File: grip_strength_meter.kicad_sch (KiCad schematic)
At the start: 0 parts

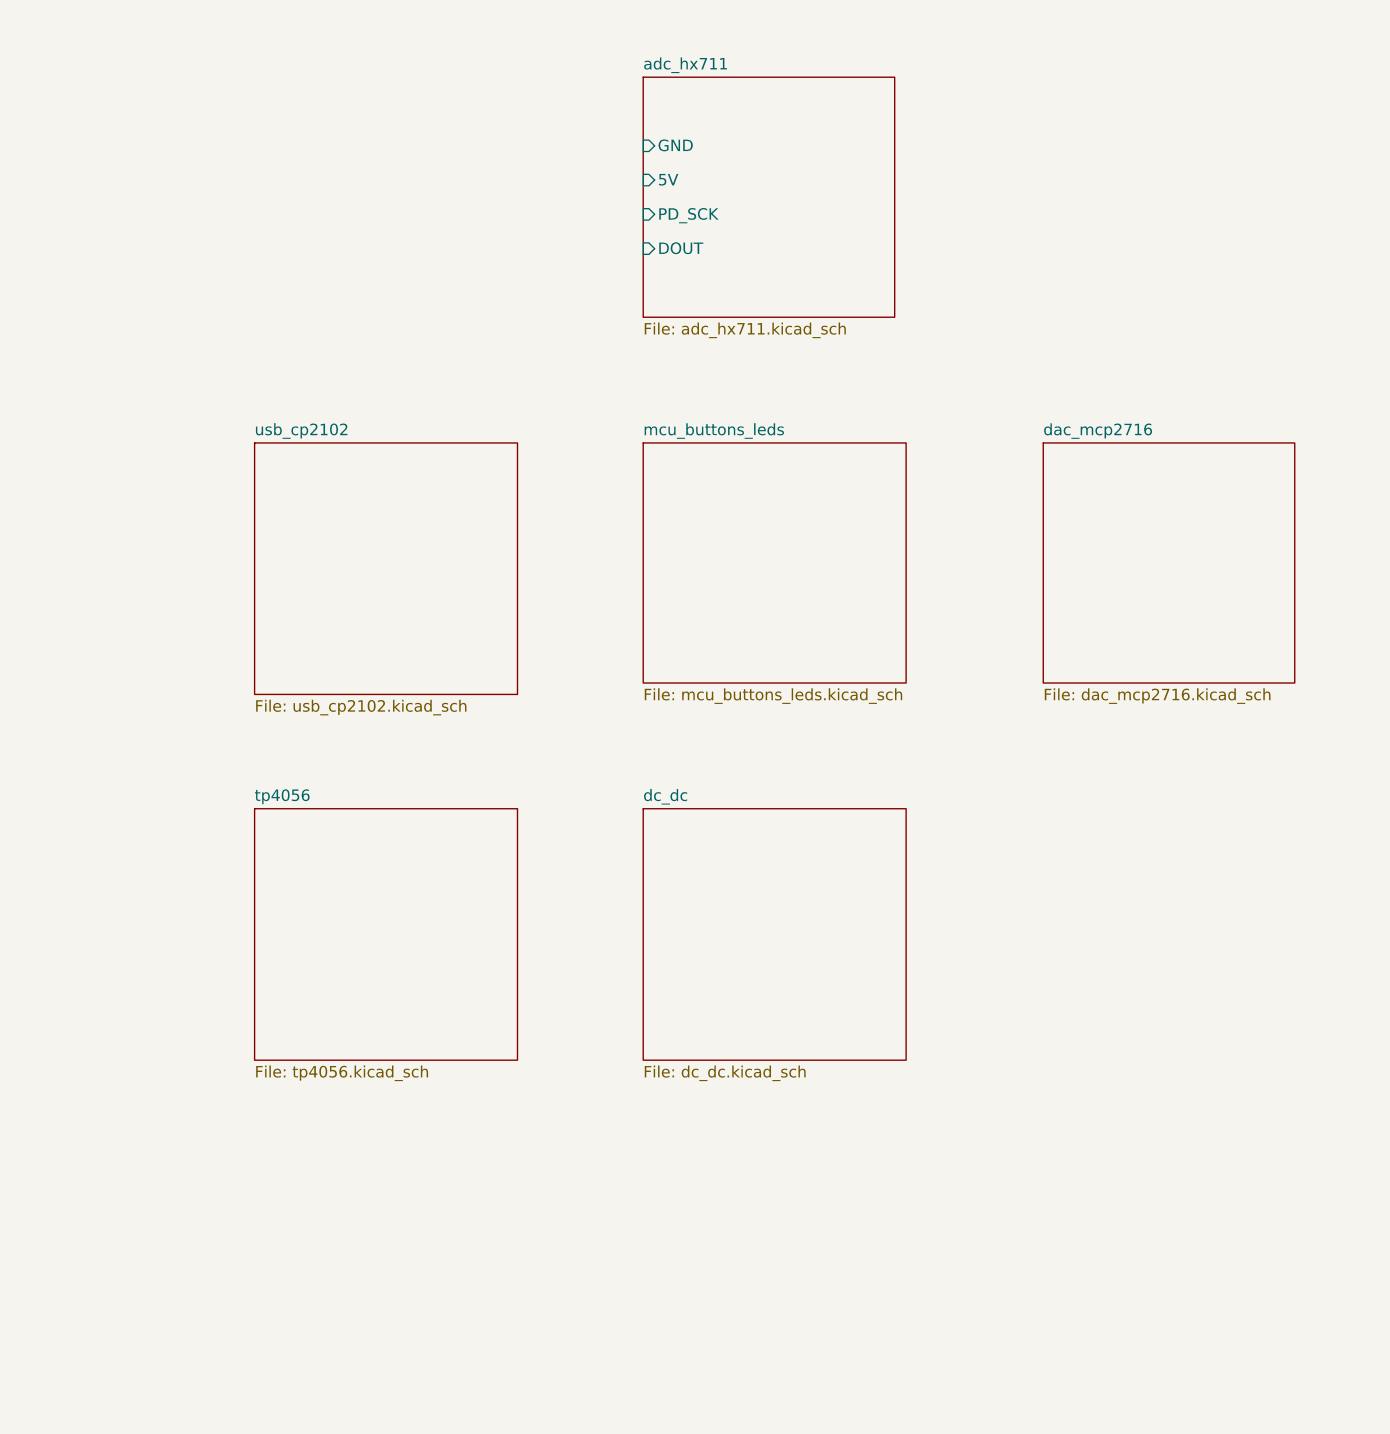
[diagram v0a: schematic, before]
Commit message: added cp2102 schematics
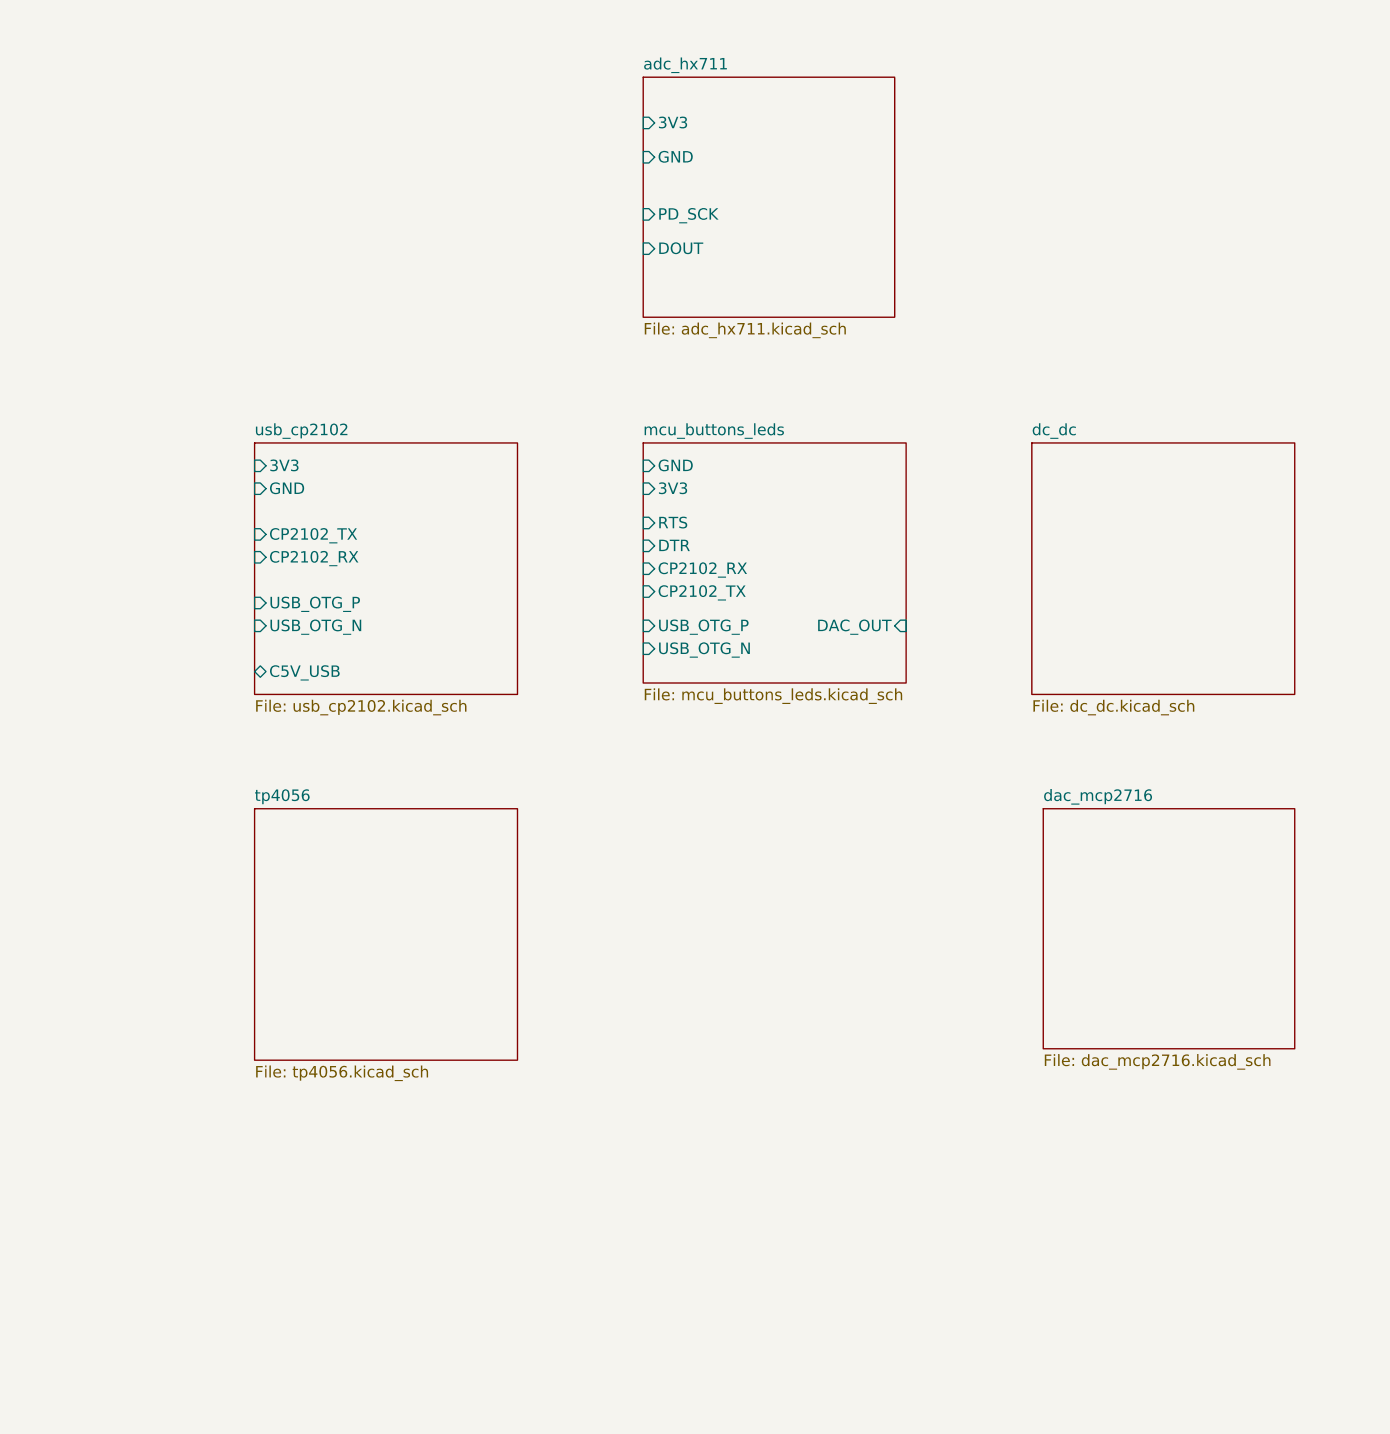
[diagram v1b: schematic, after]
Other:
- sheet adc_hx711 ports: added 3V3; removed 5V
- sheet mcu_buttons_leds ports: added 3V3, CP2102_RX, CP2102_TX, DAC_OUT, DTR, GND, RTS, USB_OTG_N, USB_OTG_P; removed none
- sheet usb_cp2102 ports: added 3V3, C5V_USB, CP2102_RX, CP2102_TX, GND, USB_OTG_N, USB_OTG_P; removed none
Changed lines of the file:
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@@
       (effects (font (size 1.27 1.27)) (justify left top))
+    )
+    (pin "GND" input (at 92.71 82.55 180)
+      (effects (font (size 1.27 1.27)) (justify left))
+    )
+    (pin "3V3" input (at 92.71 85.09 180)
+      (effects (font (size 1.27 1.27)) (justify left))
+    )
+    (pin "RTS" input (at 92.71 88.9 180)
+      (effects (font (size 1.27 1.27)) (justify left))
+    )
+    (pin "DTR" input (at 92.71 91.44 180)
+      (effects (font (size 1.27 1.27)) (justify left))
+    )
+    (pin "DAC_OUT" input (at 121.92 100.33 0)
+      (effects (font (size 1.27 1.27)) (justify right))
+    )
+    (pin "USB_OTG_P" input (at 92.71 100.33 180)
+      (effects (font (size 1.27 1.27)) (justify left))
+    )
+    (pin "USB_OTG_N" input (at 92.71 102.87 180)
+      (effects (font (size 1.27 1.27)) (justify left))
+    )
+    (pin "CP2102_RX" input (at 92.71 93.98 180)
+      (effects (font (size 1.27 1.27)) (justify left))
+    )
+    (pin "CP2102_TX" input (at 92.71 96.52 180)
+      (effects (font (size 1.27 1.27)) (justify left))
     )
     (instances
@@
     )
   )
-  (sheet (at 92.71 120.65) (size 29.21 27.94) (fields_autoplaced)
+  (sheet (at 135.89 80.01) (size 29.21 27.94) (fields_autoplaced)
     (stroke (width 0.1524) (type solid))
     (fill (color 0 0 0 0.0000))
-    (property "Sheetname" "dc_dc" (at 92.71 119.9384 0)
+    (property "Sheetname" "dc_dc" (at 135.89 79.2984 0)
       (effects (font (size 1.27 1.27)) (justify left bottom))
     )
-    (property "Sheetfile" "dc_dc.kicad_sch" (at 92.71 149.1746 0)
+    (property "Sheetfile" "dc_dc.kicad_sch" (at 135.89 108.5346 0)
       (effects (font (size 1.27 1.27)) (justify left top))
     )
@@
     )
   )
-  (sheet (at 137.16 80.01) (size 27.94 26.67) (fields_autoplaced)
+  (sheet (at 137.16 120.65) (size 27.94 26.67) (fields_autoplaced)
     (stroke (width 0.1524) (type solid))
     (fill (color 0 0 0 0.0000))
-    (property "Sheetname" "dac_mcp2716" (at 137.16 79.2984 0)
+    (property "Sheetname" "dac_mcp2716" (at 137.16 119.9384 0)
       (effects (font (size 1.27 1.27)) (justify left bottom))
     )
-    (property "Sheetfile" "dac_mcp2716.kicad_sch" (at 137.16 107.2646 0)
+    (property "Sheetfile" "dac_mcp2716.kicad_sch" (at 137.16 147.9046 0)
       (effects (font (size 1.27 1.27)) (justify left top))
     )
@@
       (effects (font (size 1.27 1.27)) (justify left top))
     )
-    (pin "GND" input (at 92.71 46.99 180)
-      (effects (font (size 1.27 1.27)) (justify left))
-    )
-    (pin "5V" input (at 92.71 50.8 180)
+    (pin "GND" input (at 92.71 48.26 180)
       (effects (font (size 1.27 1.27)) (justify left))
     )
@@
     )
     (pin "DOUT" input (at 92.71 58.42 180)
+      (effects (font (size 1.27 1.27)) (justify left))
+    )
+    (pin "3V3" input (at 92.71 44.45 180)
       (effects (font (size 1.27 1.27)) (justify left))
     )
@@
       (effects (font (size 1.27 1.27)) (justify left top))
     )
+    (pin "3V3" input (at 49.53 82.55 180)
+      (effects (font (size 1.27 1.27)) (justify left))
+    )
+    (pin "GND" input (at 49.53 85.09 180)
+      (effects (font (size 1.27 1.27)) (justify left))
+    )
+    (pin "USB_OTG_P" input (at 49.53 97.79 180)
+      (effects (font (size 1.27 1.27)) (justify left))
+    )
+    (pin "C5V_USB" bidirectional (at 49.53 105.41 180)
+      (effects (font (size 1.27 1.27)) (justify left))
+    )
+    (pin "USB_OTG_N" input (at 49.53 100.33 180)
+      (effects (font (size 1.27 1.27)) (justify left))
+    )
+    (pin "CP2102_TX" input (at 49.53 90.17 180)
+      (effects (font (size 1.27 1.27)) (justify left))
+    )
+    (pin "CP2102_RX" input (at 49.53 92.71 180)
+      (effects (font (size 1.27 1.27)) (justify left))
+    )
     (instances

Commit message: schematics almost finished
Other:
- removed sheet dc_dc
- sheet tp4056 ports: added 3V3, C5V_USB, GND, GPIO_BUTTON_CHECK, GPIO_POWEROFF, V_BAT, V_BAT_MEASURE; removed none
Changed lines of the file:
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@@
     )
   )
-  (sheet (at 49.53 120.65) (size 29.21 27.94) (fields_autoplaced)
+  (sheet (at 137.16 80.01) (size 29.21 27.94) (fields_autoplaced)
     (stroke (width 0.1524) (type solid))
     (fill (color 0 0 0 0.0000))
-    (property "Sheetname" "tp4056" (at 49.53 119.9384 0)
+    (property "Sheetname" "tp4056" (at 137.16 79.2984 0)
       (effects (font (size 1.27 1.27)) (justify left bottom))
     )
-    (property "Sheetfile" "tp4056.kicad_sch" (at 49.53 149.1746 0)
+    (property "Sheetfile" "tp4056.kicad_sch" (at 137.16 108.5346 0)
       (effects (font (size 1.27 1.27)) (justify left top))
+    )
+    (pin "GPIO_BUTTON_CHECK" input (at 137.16 82.55 180)
+      (effects (font (size 1.27 1.27)) (justify left))
+    )
+    (pin "GPIO_POWEROFF" input (at 137.16 85.09 180)
+      (effects (font (size 1.27 1.27)) (justify left))
+    )
+    (pin "C5V_USB" bidirectional (at 137.16 87.63 180)
+      (effects (font (size 1.27 1.27)) (justify left))
+    )
+    (pin "GND" input (at 137.16 90.17 180)
+      (effects (font (size 1.27 1.27)) (justify left))
+    )
+    (pin "3V3" input (at 137.16 92.71 180)
+      (effects (font (size 1.27 1.27)) (justify left))
+    )
+    (pin "V_BAT" input (at 137.16 95.25 180)
+      (effects (font (size 1.27 1.27)) (justify left))
+    )
+    (pin "V_BAT_MEASURE" input (at 137.16 97.79 180)
+      (effects (font (size 1.27 1.27)) (justify left))
     )
     (instances
@@
       )
     )
-  )
-  (sheet (at 135.89 80.01) (size 29.21 27.94) (fields_autoplaced)
-    (stroke (width 0.1524) (type solid))
-    (fill (color 0 0 0 0.0000))
-    (property "Sheetname" "dc_dc" (at 135.89 79.2984 0)
-      (effects (font (size 1.27 1.27)) (justify left bottom))
-    )
-    (property "Sheetfile" "dc_dc.kicad_sch" (at 135.89 108.5346 0)
-      (effects (font (size 1.27 1.27)) (justify left top))
-    )
-    (instances
-      (project "grip_strength_meter"
-        (path "/1f4b217c-5456-4c03-a123-3ef9839449c6" (page "5"))
-      )
-    )

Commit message: pre pre production
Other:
- sheet mcu_buttons_leds ports: added DOUT, GPIO_BUTTON_CHECK, GPIO_POWEROFF, PD_SCK, V_BAT_MEASURE; removed none
- sheet usb_cp2102 ports: added DTR, RTS; removed none
